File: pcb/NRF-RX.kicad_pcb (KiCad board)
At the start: 2 copper layers, 27 parts, among them J1 Conn_01x04_Female, J10 CH7, J11 CH8, J12 CH4, J13 CH4, J2 Conn_01x04_Female, J3 BIND, J4 CH1, J5 CH2, J6 CH3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

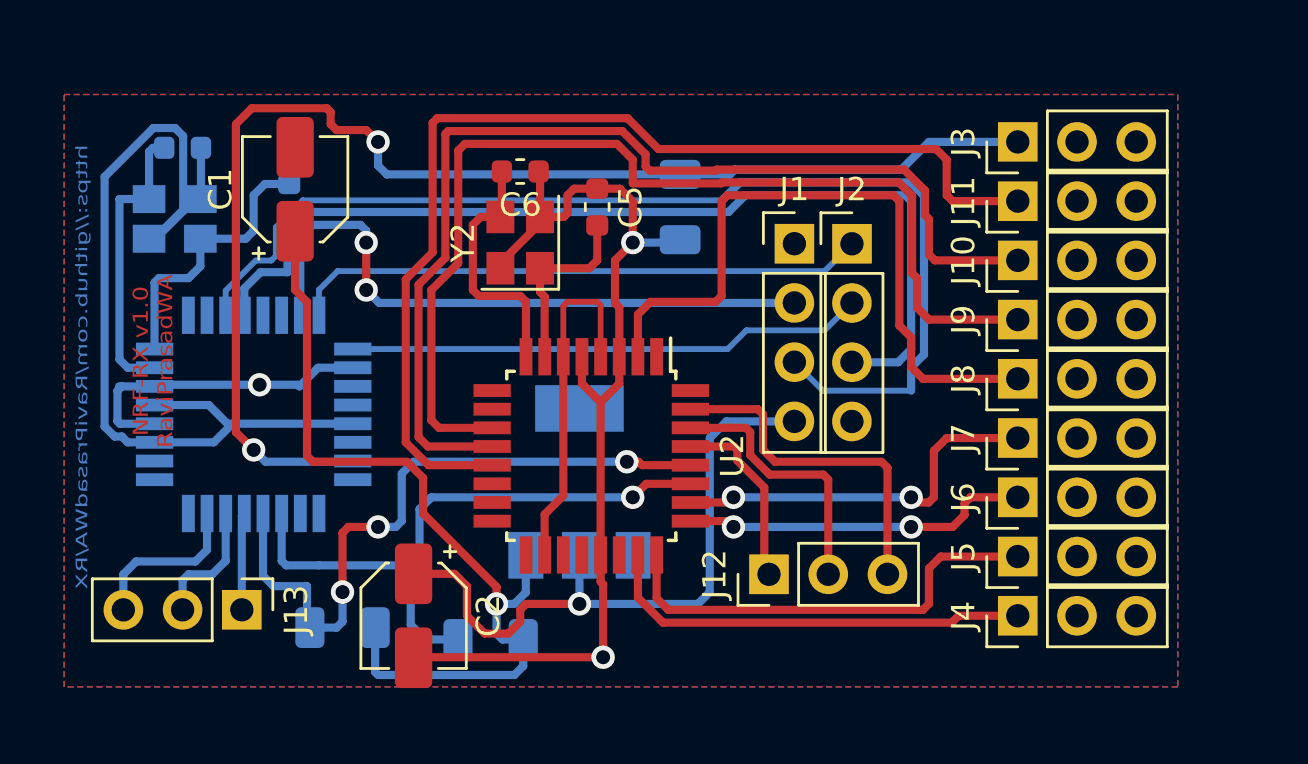
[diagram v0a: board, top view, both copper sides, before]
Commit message: added the updated PCB file for the calculated size
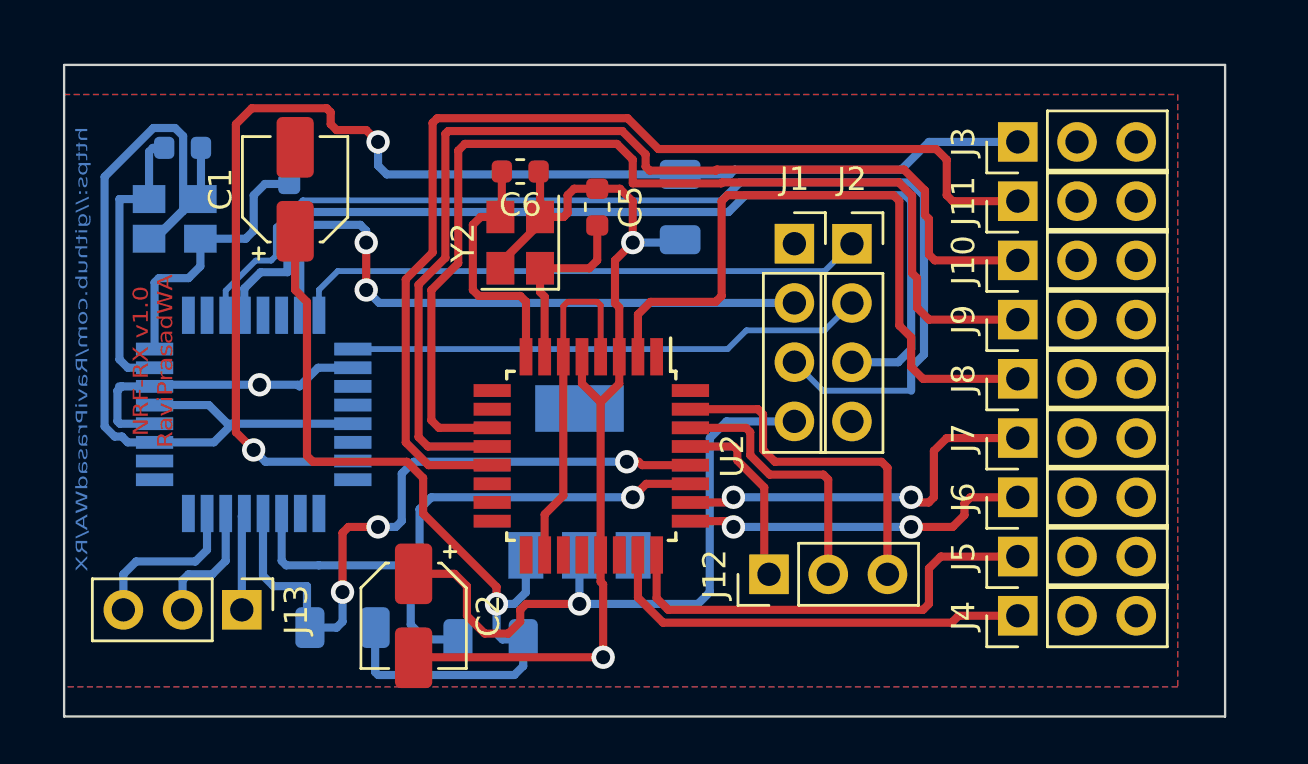
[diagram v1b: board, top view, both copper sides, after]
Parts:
- J1, J2: footprint Connector_PinHeader_2.54mm:PinHeader_1x04_P2.54mm_Vertical -> Connector_PinSocket_2.54mm:PinSocket_1x04_P2.54mm_Vertical
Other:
- board outline added: 49.8 x 27.9 mm

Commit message: added the changes
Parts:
- added C7: CP, Capacitor_SMD:CP_Elec_5x5.4, F.Cu at (137.1, 94.4)
- added C8: CP, Capacitor_SMD:CP_Elec_5x5.4, F.Cu at (159.6, 94.8)
- added U4: LM1117-5.0, Package_TO_SOT_SMD:SOT-223, F.Cu at (142.0, 102.4)
- moved Y2 0.14 mm to (152.8, 96.5)
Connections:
- C1 pad 1: +5V -> Net-(C1-Pad1)
- J3 pad 2: +5V -> Net-(C1-Pad1)
- R1 pad 2: +5V -> Net-(C1-Pad1)
- R2 pad 2: +5V -> Net-(C1-Pad1)
- U1 pad 18: +5V -> Net-(C1-Pad1)
- U1 pad 4: +5V -> Net-(C1-Pad1)
- U1 pad 6: +5V -> Net-(C1-Pad1)
- U2 pad 18: +5V -> Net-(C1-Pad1)
- U2 pad 4: +5V -> Net-(C1-Pad1)
- U2 pad 6: +5V -> Net-(C1-Pad1)
- U3 pad 3: +5V -> Net-(C1-Pad1)
- Y1 pad 4: GND -> (no net)
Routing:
- net Net-(C1-Pad1): track 0.00 -> 143.3 mm, vias 0 -> 2
- net GND: track 83.2 -> 106.0 mm, vias 2 -> 5
- net Net-(J11-Pad1): track 45.8 -> 50.5 mm, vias 0 -> 2
- net +5V: track 65.7 -> 70.1 mm, vias 2 -> 0
- net Net-(J10-Pad1): track 45.5 -> 49.3 mm, vias 0 -> 2
- net Net-(J9-Pad1): track 45.3 -> 49.0 mm, vias 0 -> 2
- net Net-(J3-Pad1): track 55.2 -> 53.7 mm
